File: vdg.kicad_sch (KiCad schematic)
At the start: 3 parts, among them IC12 MC6847, IC13 74LS273N

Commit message: add video padding circuit
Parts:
- added C11: 4.7uF, Capacitor_THT:CP_Radial_Tantal_D5.5mm_P5.00mm, symbol Device:C_Polarized_Small
- C36: footprint Capacitor_THT:CP_Radial_D6.3mm_P2.50mm -> Capacitor_THT:CP_Radial_D8.0mm_P5.00mm
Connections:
- net +5V: now also C11.1
- net GND: now also C11.2
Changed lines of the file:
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@@
+	(symbol
+		(lib_id "power:GND")
+		(at 143.51 43.18 270)
+		(unit 1)
+		(exclude_from_sim no)
+		(in_bom yes)
+		(on_board yes)
+		(dnp no)
+		(property "Reference" "#PWR0171"
+			(at 137.16 43.18 0)
+			(effects
+				(font
+					(size 1.27 1.27)
+				)
+				(hide yes)
+			)
+		)
+		(property "Value" "GND"
+			(at 137.16 41.91 90)
+			(effects
+				(font
+					(size 1.27 1.27)
+				)
+				(justify left)
+			)
+		)
+		(property "Footprint" ""
+			(at 143.51 43.18 0)
+			(effects
+				(font
+					(size 1.27 1.27)
+				)
+				(hide yes)
+			)
+		)
+		(property "Datasheet" ""
+			(at 143.51 43.18 0)
+			(effects
+				(font
+					(size 1.27 1.27)
+				)
+				(hide yes)
+			)
+		)
+		(property "Description" ""
+			(at 143.51 43.18 0)
+			(effects
+				(font
+					(size 1.27 1.27)
+				)
+				(hide yes)
+			)
+		)
+		(pin "1"
+		)
+		(instances
+			(project "Dragon32Issue2ASecam"
+				(path "/e3d9e4a2-26cb-4482-98c1-138d9a22d1eb/92f4f63c-278c-488a-b182-7bfdf4d90c3e"
+					(reference "#PWR0171")
+					(unit 1)
+				)
+			)
+		)
+	)
 	(symbol
 		(lib_id "power:GND")
@@
 				(path "/e3d9e4a2-26cb-4482-98c1-138d9a22d1eb/92f4f63c-278c-488a-b182-7bfdf4d90c3e"
 					(reference "#PWR0117")
+					(unit 1)
+				)
+			)
+		)
+	)
+	(symbol
+		(lib_id "power:+5V")
+		(at 148.59 43.18 0)
+		(unit 1)
+		(exclude_from_sim no)
+		(in_bom yes)
+		(on_board yes)
+		(dnp no)
+		(fields_autoplaced yes)
+		(property "Reference" "#PWR0168"
+			(at 148.59 46.99 0)
+			(effects
+				(font
+					(size 1.27 1.27)
+				)
+				(hide yes)
+			)
+		)
+		(property "Value" "+5V"
+			(at 148.59 37.846 0)
+			(effects
+				(font
+					(size 1.27 1.27)
+				)
+			)
+		)
+		(property "Footprint" ""
+			(at 148.59 43.18 0)
+			(effects
+				(font
+					(size 1.27 1.27)
+				)
+				(hide yes)
+			)
+		)
+		(property "Datasheet" ""
+			(at 148.59 43.18 0)
+			(effects
+				(font
+					(size 1.27 1.27)
+				)
+				(hide yes)
+			)
+		)
+		(property "Description" ""
+			(at 148.59 43.18 0)
+			(effects
+				(font
+					(size 1.27 1.27)
+				)
+				(hide yes)
+			)
+		)
+		(pin "1"
+		)
+		(instances
+			(project "Dragon32Issue2ASecam"
+				(path "/e3d9e4a2-26cb-4482-98c1-138d9a22d1eb/92f4f63c-278c-488a-b182-7bfdf4d90c3e"
+					(reference "#PWR0168")
 					(unit 1)
 				)
@@
 			)
 		)
-		(property "Footprint" "Capacitor_THT:CP_Radial_D6.3mm_P2.50mm"
+		(property "Footprint" "Capacitor_THT:CP_Radial_D8.0mm_P5.00mm"
 			(at 146.558 59.563 0)
 			(effects
@@
 					(unit 1)
 				)
+			)
+		)
+	)
+	(symbol
+		(lib_id "Device:C_Polarized_Small")
+		(at 146.05 43.18 270)
+		(unit 1)
+		(exclude_from_sim no)
+		(in_bom yes)
+		(on_board yes)
+		(dnp no)
+		(property "Reference" "C11"
+			(at 149.479 45.974 90)
+			(effects
+				(font
+					(size 1.27 1.27)
+				)
+				(justify right)
+			)
+		)
+		(property "Value" "4.7uF"
+			(at 151.13 47.879 90)
+			(effects
+				(font
+					(size 1.27 1.27)
+				)
+				(justify right)
+			)
+		)
+		(property "Footprint" "Capacitor_THT:CP_Radial_Tantal_D5.5mm_P5.00mm"
+			(at 146.05 43.18 0)
+			(effects
+				(font
+					(size 1.27 1.27)
+				)
+				(hide yes)
+			)
+		)
+		(property "Datasheet" "https://datasheets.kyocera-avx.com/tap.pdf"
+			(at 146.05 43.18 0)
+			(effects
+				(font
+					(size 1.27 1.27)
+				)
+				(hide yes)
+			)
+		)
+		(property "Description" ""
+			(at 146.05 43.18 0)
+			(effects
+				(font
+					(size 1.27 1.27)
+				)
+				(hide yes)
+			)
+		)
+		(property "DigiKey" "478-8984-1-ND"
+			(at 146.05 43.18 90)
+			(effects
+				(font
+					(size 1.27 1.27)
+				)
+				(hide yes)
+			)
+		)
+		(pin "1"
+		)
+		(pin "2"
+		)
+		(instances
+			(project "Dragon32Issue2ASecam"
+				(path "/e3d9e4a2-26cb-4482-98c1-138d9a22d1eb/92f4f63c-278c-488a-b182-7bfdf4d90c3e"
+					(reference "C11")
+					(unit 1)
+				)

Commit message: video circuit tracing
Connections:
- net DO0: now also IC13.13 (D4); no longer IC13.3 (D0)
- net DO1: now also IC13.8 (D3); no longer IC13.4 (D1)
- net DO2: now also IC13.3 (D0); no longer IC13.7 (D2)
- net DO3: now also IC13.7 (D2); no longer IC13.8 (D3)
- net DO4: now also IC13.4 (D1); no longer IC13.13 (D4)
- net DO5: now also IC13.17 (D6); no longer IC13.14 (D5)
- net DO6: now also IC13.18 (D7); no longer IC13.17 (D6)
- net DO7: now also IC13.14 (D5); no longer IC13.18 (D7)
- net GD0: now also IC13.12 (Q4); no longer IC13.2 (Q0)
- net GD1: now also IC13.9 (Q3); no longer IC13.5 (Q1)
- net GD2: now also IC13.2 (Q0); no longer IC13.6 (Q2)
- net GD3: now also IC13.6 (Q2); no longer IC13.9 (Q3)
- net GD4: now also IC13.5 (Q1); no longer IC13.12 (Q4)
- net GD5: now also IC13.16 (Q6); no longer IC13.15 (Q5)
- net GD6: now also IC13.19 (Q7); no longer IC13.16 (Q6)
- net GD7: now also IC13.15 (Q5); no longer IC13.19 (Q7)
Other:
- moved on the sheet: IC13

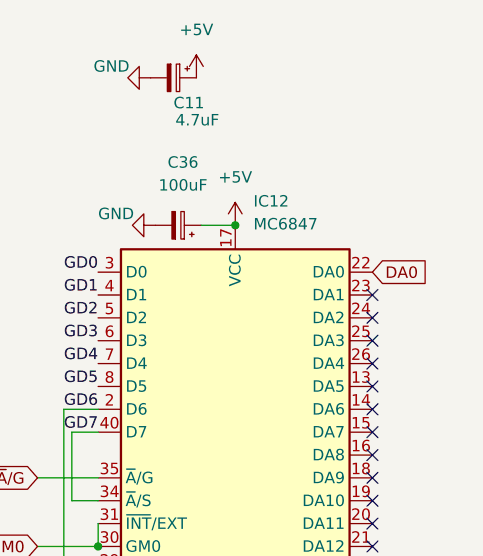
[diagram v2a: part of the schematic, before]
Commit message: FM generator routing
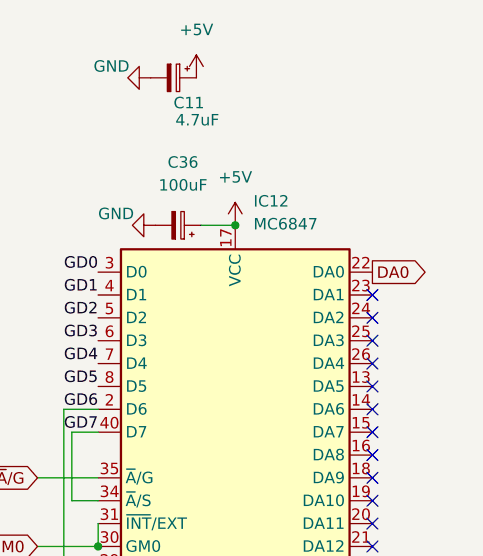
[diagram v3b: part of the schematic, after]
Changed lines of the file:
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@@
 	)
 	(global_label "DA0"
-		(shape input)
+		(shape output)
 		(at 168.148 64.77 0)
 		(fields_autoplaced yes)
@@
 		)
 		(property "Intersheetrefs" "${INTERSHEET_REFS}"
-			(at 174.0403 64.6906 0)
+			(at 174.7013 64.77 0)
 			(effects
 				(font
